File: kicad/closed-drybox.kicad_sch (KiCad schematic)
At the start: 16 parts, among them J1 Conn_01x02, J10 Conn_01x02_Pin, J2 Power_Jack, J3 Conn_01x02_Pin, J5 Conn_01x02_Pin, J6 Conn_01x05_Pin, J7 Conn_01x02, J8 Conn_01x02, J9 Conn_02x04_Odd_Even, U2 XIAO-ESP32-C6

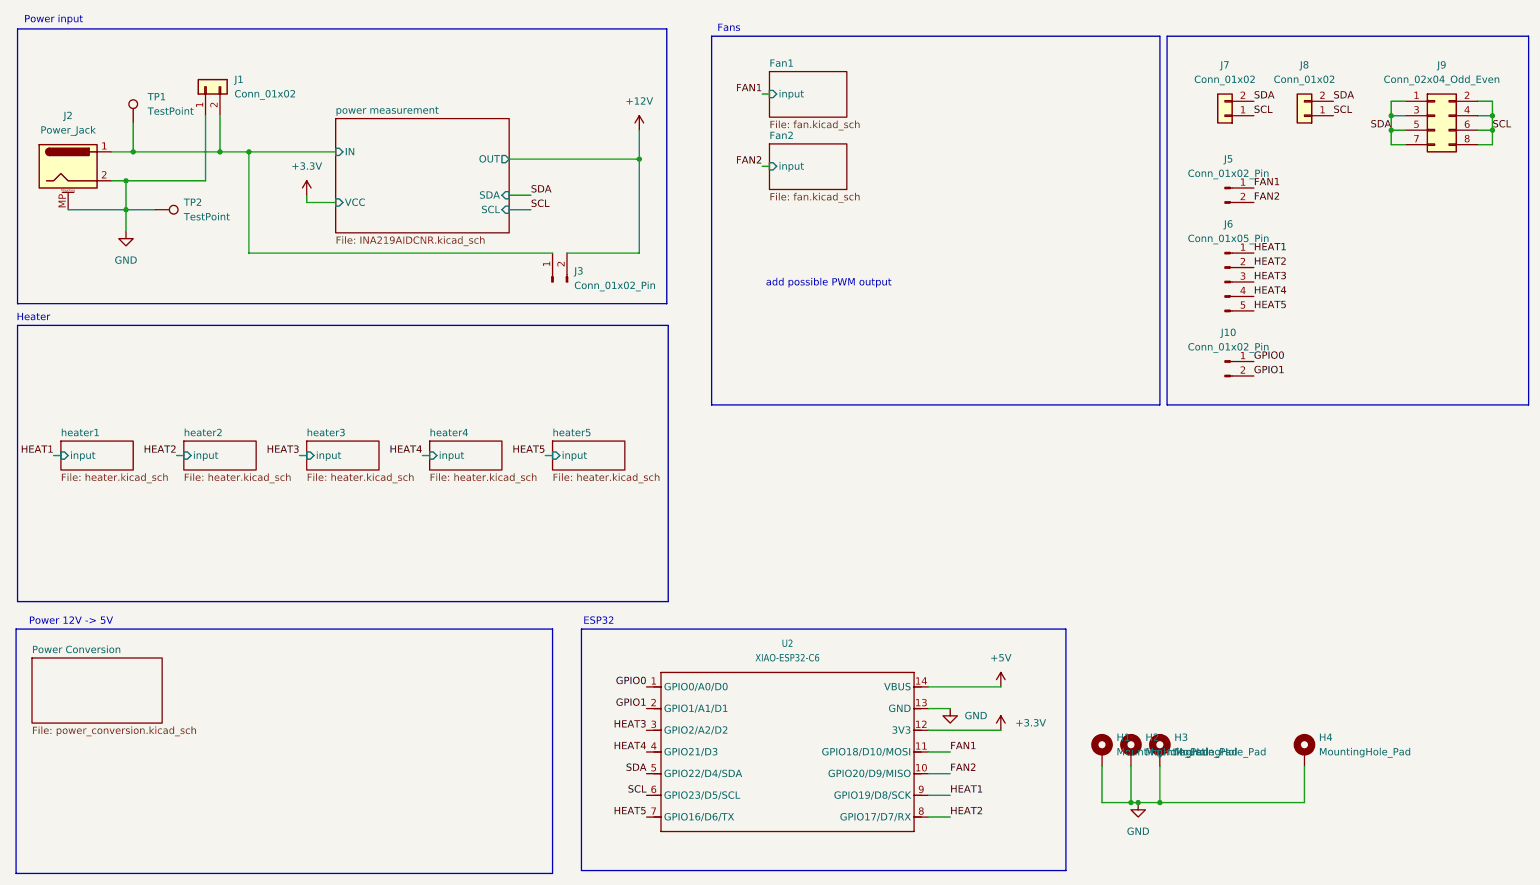
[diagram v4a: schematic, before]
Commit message: added connectors to schematic
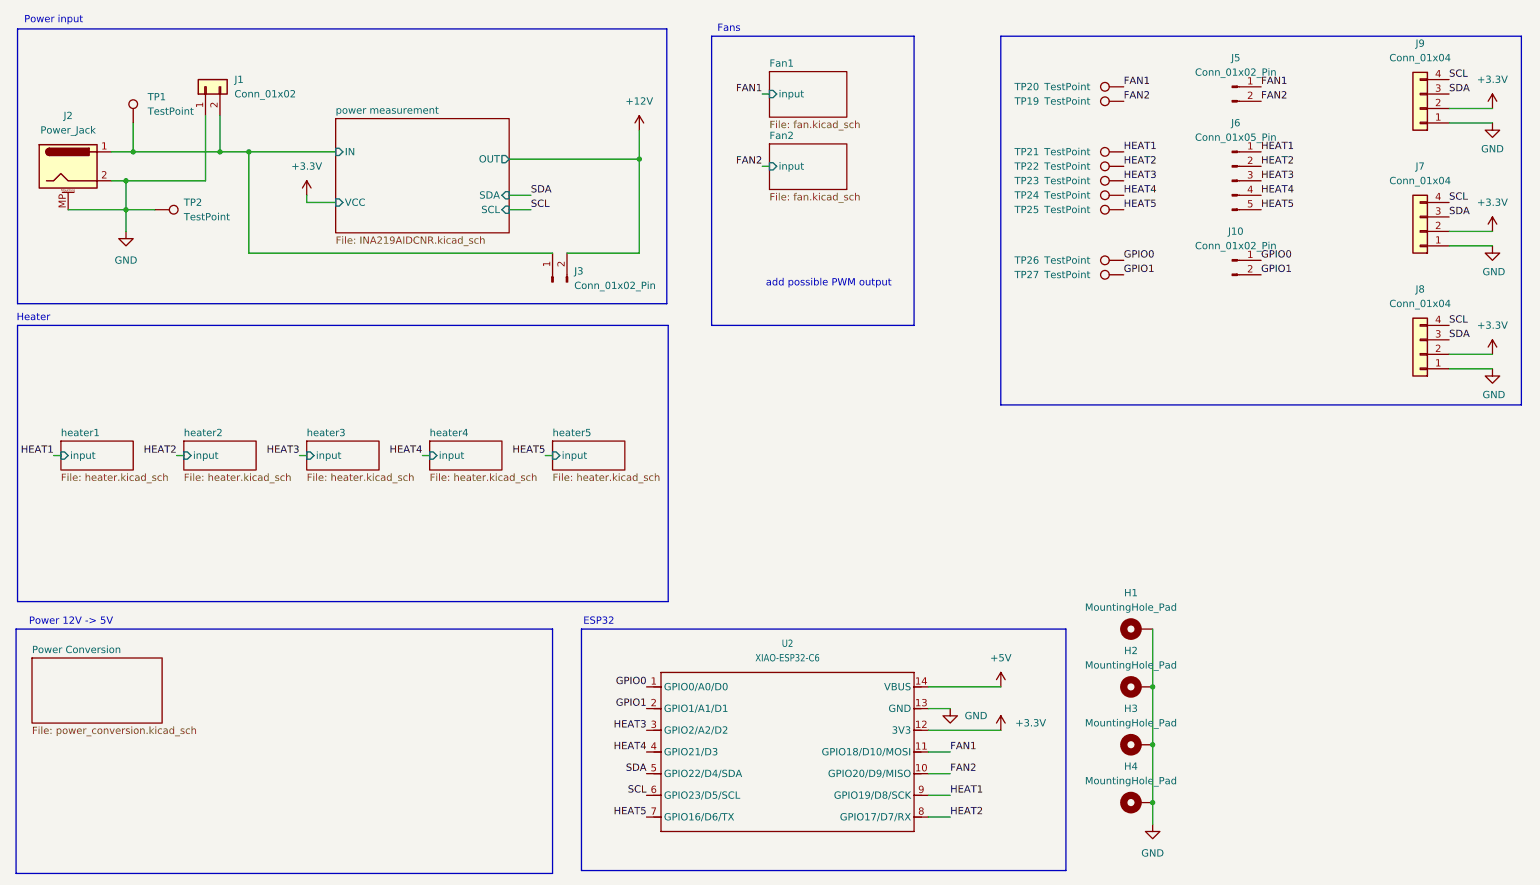
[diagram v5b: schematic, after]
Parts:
- removed J7, J8: Conn_01x02, Connector_JST:JST_XH_S2B-XH-A-1_1x02_P2.50mm_Horizontal, symbol Connector_Generic:Conn_01x02
- removed J9: Conn_02x04_Odd_Even, symbol Connector_Generic:Conn_02x04_Odd_Even
- added J7, J8, J9: Conn_01x04, Connector_JST:JST_XH_B4B-XH-AM_1x04_P2.50mm_Vertical, symbol Connector_Generic:Conn_01x04
- added TP19, TP20, TP21, TP22, TP23, TP24, TP25, TP26, TP27: TestPoint, symbol Connector:TestPoint
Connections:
- net +3.3V: now also J7.2 (Pin_2), J8.2 (Pin_2), J9.2 (Pin_2)
- net FAN1: now also TP20.1
- net FAN2: now also TP19.1
- net GND: now also J7.1 (Pin_1), J8.1 (Pin_1), J9.1 (Pin_1)
- net GPIO0: now also TP26.1
- net GPIO1: now also TP27.1
- net HEAT1: now also TP21.1
- net HEAT2: now also TP22.1
- net HEAT3: now also TP23.1
- net HEAT4: now also TP24.1
- net HEAT5: now also TP25.1
- net SCL: now also J7.4 (Pin_4), J8.4 (Pin_4), J9.4 (Pin_4)
- net SDA: now also J7.3 (Pin_3), J8.3 (Pin_3), J9.3 (Pin_3)
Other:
- moved on the sheet: J10, J5, J6

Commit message: added footprints
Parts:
- TP19, TP20, TP21, TP22, TP23, TP24, TP25, TP26, TP27: footprint (none) -> TestPoint:TestPoint_Pad_D2.5mm
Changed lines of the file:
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@@
 			)
 		)
-		(property "Footprint" ""
+		(property "Footprint" "TestPoint:TestPoint_Pad_D2.5mm"
 			(at 209.55 22.86 0)
 			(effects
@@
 			)
 		)
-		(property "Footprint" ""
+		(property "Footprint" "TestPoint:TestPoint_Pad_D2.5mm"
 			(at 209.55 34.29 0)
 			(effects
@@
 			)
 		)
-		(property "Footprint" ""
+		(property "Footprint" "TestPoint:TestPoint_Pad_D2.5mm"
 			(at 209.55 53.34 0)
 			(effects
@@
 			)
 		)
-		(property "Footprint" ""
+		(property "Footprint" "TestPoint:TestPoint_Pad_D2.5mm"
 			(at 209.55 44.45 0)
 			(effects
@@
 			)
 		)
-		(property "Footprint" ""
+		(property "Footprint" "TestPoint:TestPoint_Pad_D2.5mm"
 			(at 209.55 36.83 0)
 			(effects
@@
 			)
 		)
-		(property "Footprint" ""
+		(property "Footprint" "TestPoint:TestPoint_Pad_D2.5mm"
 			(at 209.55 39.37 0)
 			(effects
@@
 			)
 		)
-		(property "Footprint" ""
+		(property "Footprint" "TestPoint:TestPoint_Pad_D2.5mm"
 			(at 209.55 55.88 0)
 			(effects
@@
 			)
 		)
-		(property "Footprint" ""
+		(property "Footprint" "TestPoint:TestPoint_Pad_D2.5mm"
 			(at 209.55 25.4 0)
 			(effects
@@
 			)
 		)
-		(property "Footprint" ""
+		(property "Footprint" "TestPoint:TestPoint_Pad_D2.5mm"
 			(at 209.55 41.91 0)
 			(effects

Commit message: pcb design v0.2
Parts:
- removed TP19, TP2, TP20, TP21, TP22, TP23, TP24, TP25: TestPoint, TestPoint:TestPoint_Pad_D2.5mm, symbol Connector:TestPoint

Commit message: review with @lukstruck
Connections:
- net GND: now also J2.3 (MountPin); no longer J2.MP (MountPin)
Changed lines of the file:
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@@
 			)
 		)
-		(pin "MP"
+		(pin "3"
 		)
 		(pin "1"
